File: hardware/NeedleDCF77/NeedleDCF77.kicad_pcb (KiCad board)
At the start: 2 copper layers, 1 part, among them U1 MINI-M4_STM32

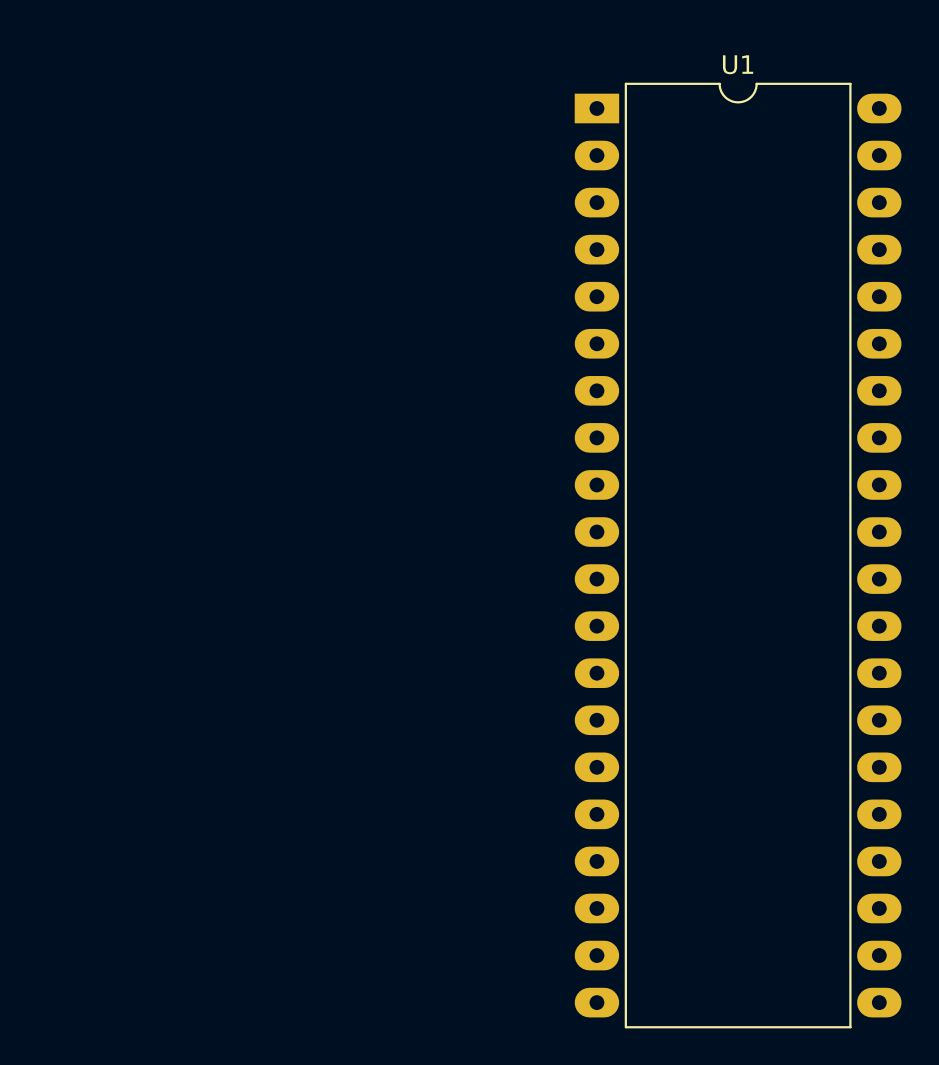
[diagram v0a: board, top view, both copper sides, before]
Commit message: Implementation of 3V
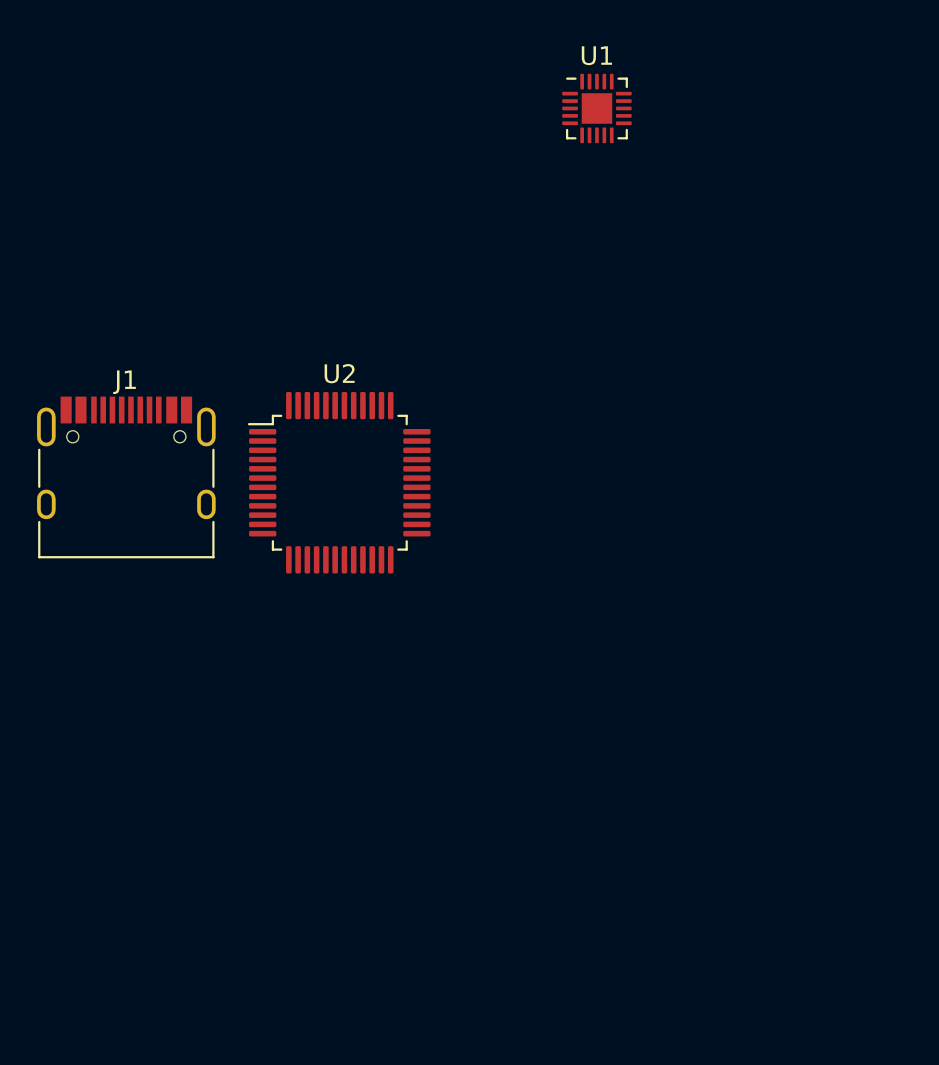
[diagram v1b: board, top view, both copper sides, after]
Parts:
- added J1: USB_C_Receptacle_USB2.0, Connector_USB:USB_C_Receptacle_HRO_TYPE-C-31-M-12, F.Cu at (114.3, 83.8)
- added U2: STM32L051C8Tx, Package_QFP:LQFP-48_7x7mm_P0.5mm, F.Cu at (125.8, 83.7)
- U1: value MINI-M4_STM32 -> LTC3558; footprint Package_DIP:DIP-40_W15.24mm_LongPads -> Package_DFN_QFN:QFN-20-1EP_3x3mm_P0.4mm_EP1.65x1.65mm
